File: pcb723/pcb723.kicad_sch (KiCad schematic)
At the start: 57 parts, among them J1 Conn_01x02_Pin, J2 Conn_01x02_Pin, J3 Conn_02x07_Odd_Even, J4 Conn_02x04_Odd_Even, J5 USB_C_Receptacle_USB2.0_16P, SW1 SW_Push, U1 STM32H723ZGT6, U2 AMS1117-3.3, Y1 8MHz 20pF

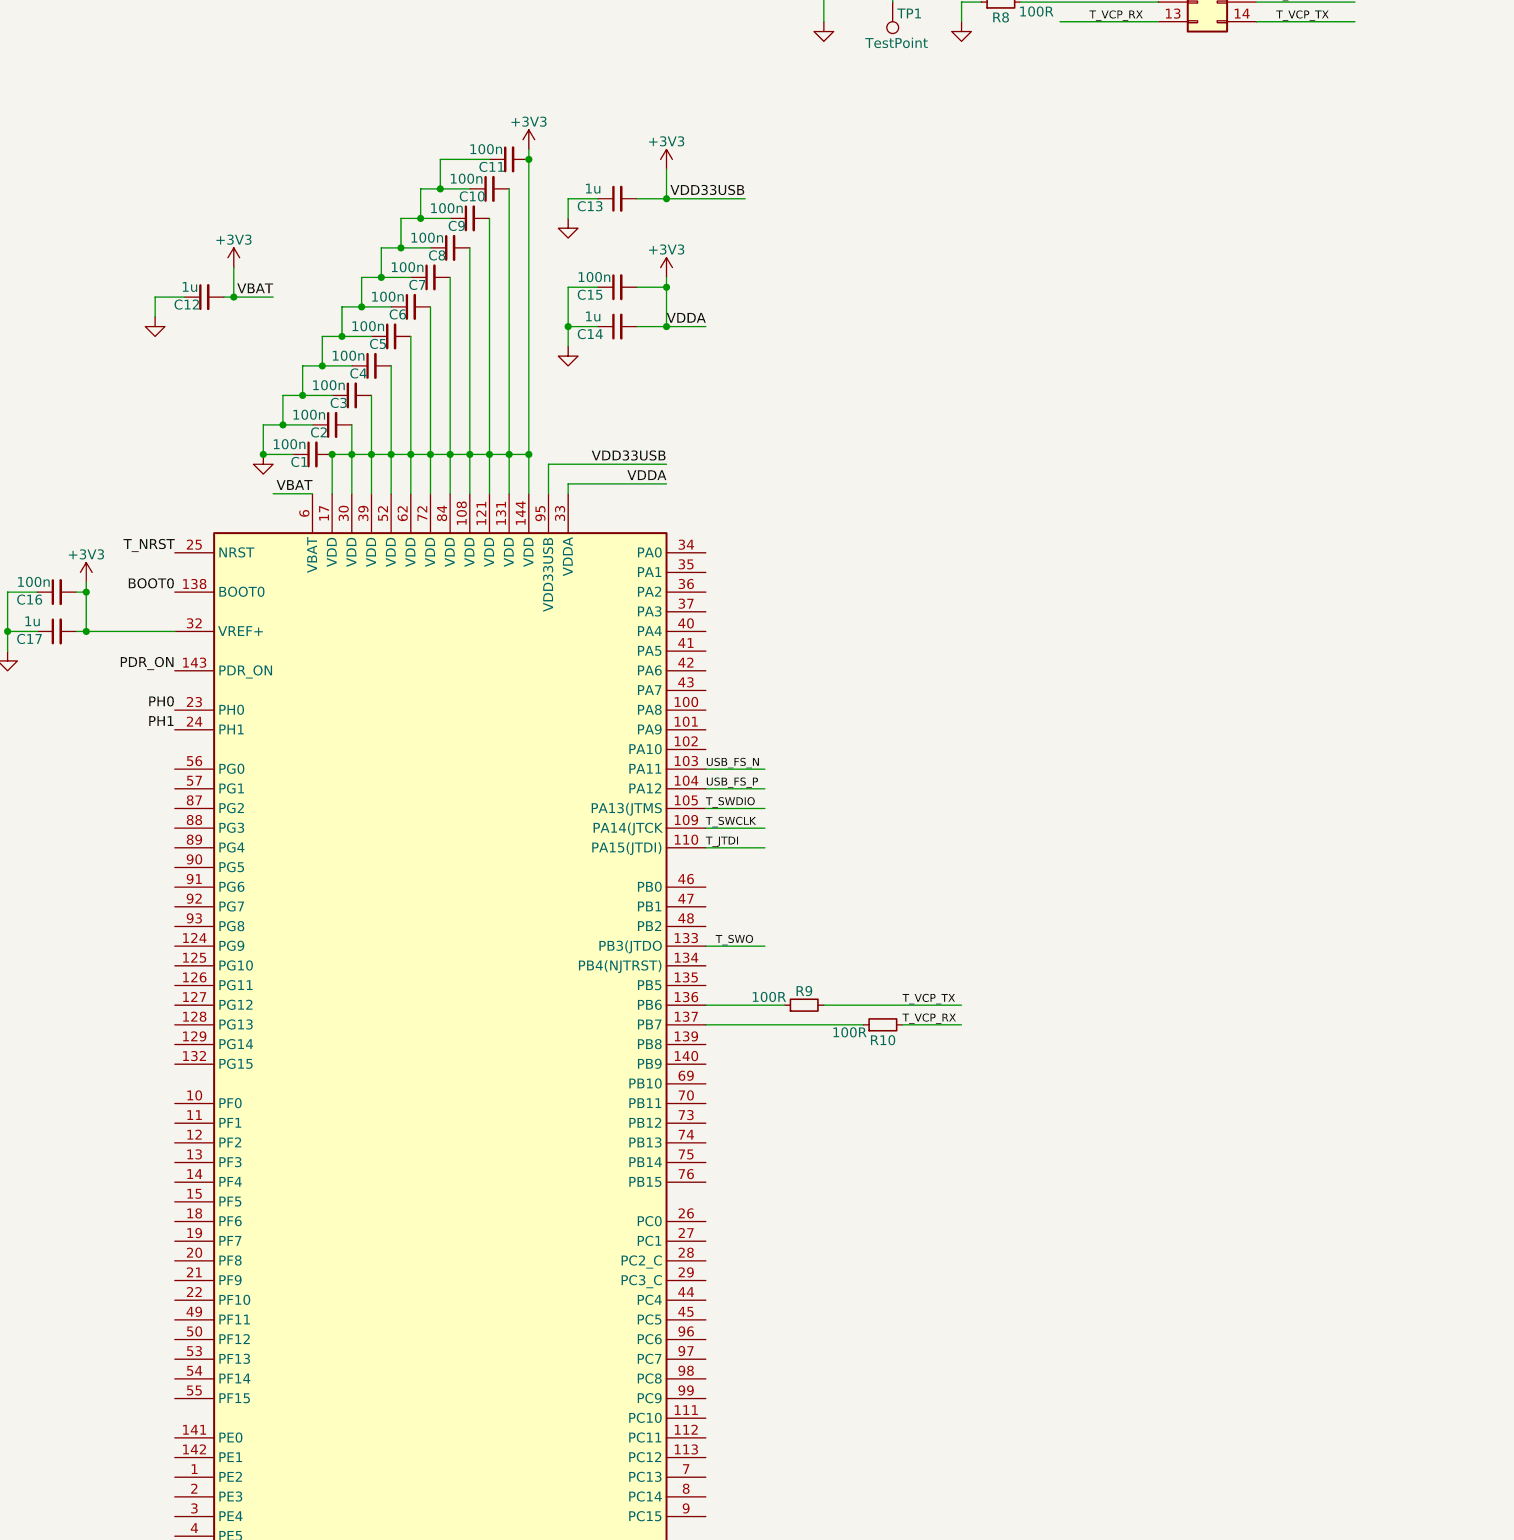
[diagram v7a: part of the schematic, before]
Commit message: Add 26 pin breakout
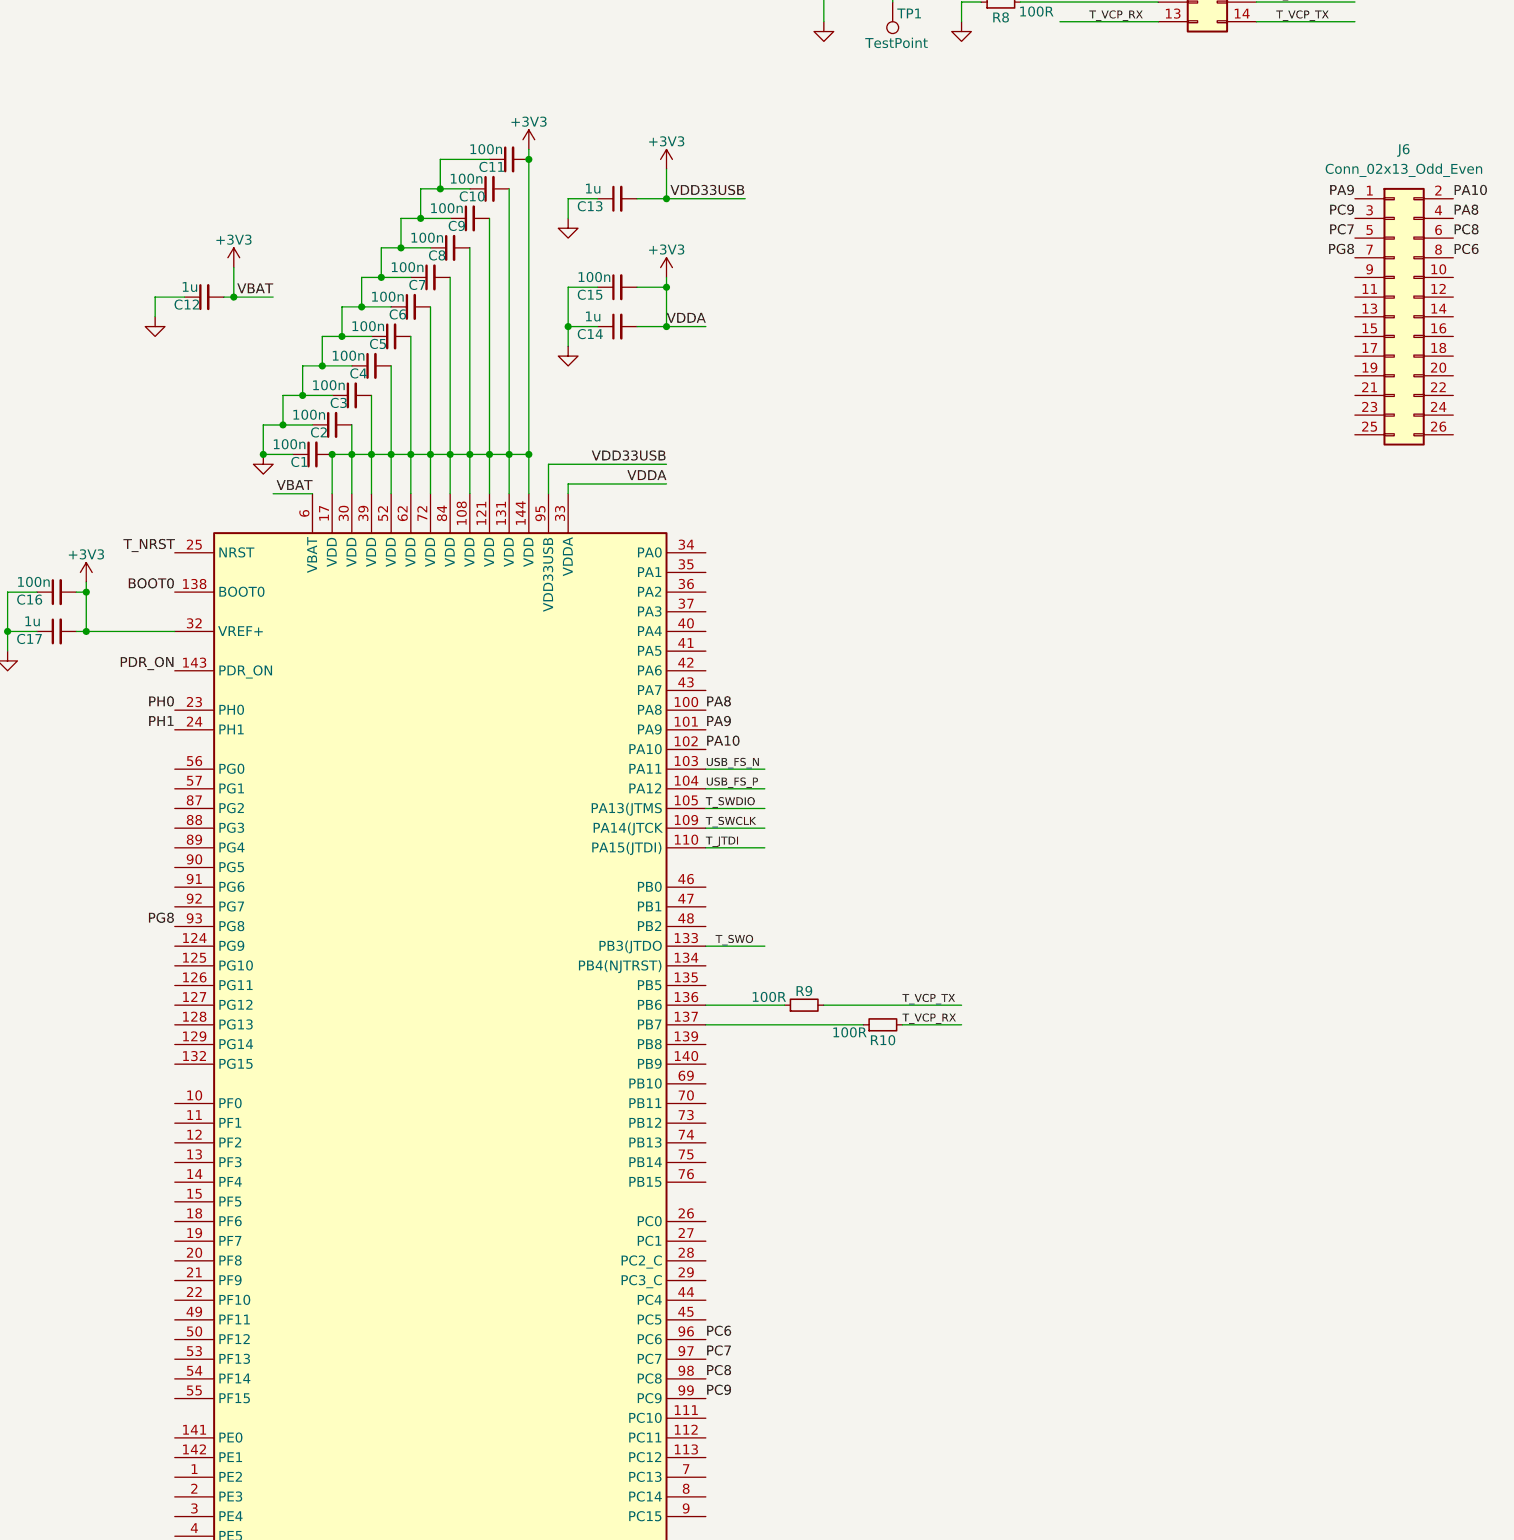
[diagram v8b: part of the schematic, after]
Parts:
- added J6: Conn_02x13_Odd_Even, Connector_PinSocket_2.54mm:PinSocket_2x13_P2.54mm_Vertical, symbol Connector_Generic:Conn_02x13_Odd_Even
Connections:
- net PA8: now reaches U1.100 (PA8)
- net PA8: now also J6.4 (Pin_4)
- net PA9: now reaches U1.101 (PA9)
- net PA9: now also J6.1 (Pin_1)
- net PA10: now reaches U1.102 (PA10)
- net PA10: now also J6.2 (Pin_2)
- net PG8: now reaches U1.93 (PG8)
- net PG8: now also J6.7 (Pin_7)
- net PC6: now reaches U1.96 (PC6)
- net PC6: now also J6.8 (Pin_8)
- net PC7: now reaches U1.97 (PC7)
- net PC7: now also J6.5 (Pin_5)
- net PC8: now reaches U1.98 (PC8)
- net PC8: now also J6.6 (Pin_6)
- net PC9: now reaches U1.99 (PC9)
- net PC9: now also J6.3 (Pin_3)
